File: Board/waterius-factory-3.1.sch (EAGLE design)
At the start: 23 parts, among them IC1 TINY85-20SU, U3 ESP01

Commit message: New attiny package
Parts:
- IC1: value TINY85-20SU -> ATTINY85-20SU; device atmel:TINY13-20SU -> attiny85:ATTINY85-20SU
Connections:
- net +3V: now also IC1P.VCC; no longer IC1.VCC
- net GND: now also IC1P.GND; no longer IC1.GND
- net IN1: now also IC1G$1.PB3(ADC3/!OC1B!/CLKI/XTAL1/PCINT3); no longer IC1.PB3/PCINT3/CLKI/ADC3
- net IN2: now also IC1G$1.PB4(ADC2/OC1B/CLKO/XTAL2/PCINT4); no longer IC1.PB4/PCINT4/ADC2
- net PRG_RST: now also IC1G$1.PB5(DW/ADC0/!RESET!/PCINT5); no longer IC1.PB5/PCINT5/!RESET!/ADC0/DW
- net SCK: now also IC1G$1.PB2(SCK/USCK/SCL/ADC1/T0/INT0/PCINT2); no longer IC1.PB2/PCINT2/SCK/ADC1/T0
- net SDA: now also IC1G$1.PB0(MOSI/DI/SDA/AIN0/OC0A/!OC1A!/AREF/PCINT0); no longer IC1.PB0/PCINT0/AIN0/OC0A/MOSI
- net WAKE_UP: now also IC1G$1.PB1(MISO/DO/AIN1/OC0B/OC1A/PCINT1); no longer IC1.PB1/PCINT1/AIN1/OC0B/INT0/MISO
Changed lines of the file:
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@@
 <part name="C4" library="rcl" deviceset="C-EU" device="C0805" value="1uF"/>
 <part name="C2" library="rcl" deviceset="C-EU" device="C0805" value="0.1uF"/>
-<part name="+3V" library="supply1" library_urn="urn:adsk.eagle:library:371" deviceset="VCC" device=""/>
+<part name="+3V" library="supply1" deviceset="VCC" device=""/>
 <part name="X1" library="con-wago255" deviceset="233-104" device=""/>
 <part name="R1" library="resistor" deviceset="R-EU_" device="R0805" value="3k3"/>
 <part name="GND1" library="supply1" deviceset="GND" device=""/>
 <part name="GND2" library="supply1" deviceset="GND" device=""/>
-<part name="+3V2" library="supply1" library_urn="urn:adsk.eagle:library:371" deviceset="VCC" device=""/>
+<part name="+3V2" library="supply1" deviceset="VCC" device=""/>
 <part name="LOG" library="pinhead" deviceset="PINHD-1X1" device=""/>
 <part name="R3" library="resistor" deviceset="R-EU_" device="R0805" value="300"/>
@@
 <part name="GND5" library="supply1" deviceset="GND" device=""/>
 <part name="RST" library="pinhead" deviceset="PINHD-1X1" device="" value="RST"/>
-<part name="IC1" library="atmel" deviceset="TINY13" device="SU" technology="-20" value="TINY85-20SU"/>
 <part name="R5" library="resistor" deviceset="R-EU_" device="R0805" value="3k3"/>
 <part name="C3" library="rcl" deviceset="C-EU" device="C0805" value="0.1uF"/>
@@
 <part name="U$1" library="MCP1700T-3002E_TT" deviceset="MCP1700T-3002E/TT" device=""/>
 <part name="S1" library="switch-omron" library_urn="urn:adsk.eagle:library:377" deviceset="31-XX" device="" package3d_urn="urn:adsk.eagle:package:27487/1"/>
+<part name="IC1" library="attiny85" deviceset="ATTINY*5" device="-20SU" technology="8"/>
 </parts>
 <sheets>
@@
 <attribute name="VALUE" x="64.77" y="25.4" size="1.778" layer="96" rot="R180"/>
 </instance>
-<instance part="IC1" gate="G$1" x="109.22" y="22.86" smashed="yes">
-<attribute name="NAME" x="91.44" y="39.37" size="1.778" layer="95"/>
-<attribute name="VALUE" x="91.44" y="12.7" size="1.778" layer="96"/>
-</instance>
 <instance part="R5" gate="G$1" x="76.2" y="45.72" smashed="yes" rot="R90">
 <attribute name="NAME" x="74.7014" y="41.91" size="1.778" layer="95" rot="R90"/>
@@
 <attribute name="NAME" x="36.83" y="27.305" size="1.778" layer="95" rot="MR270"/>
 <attribute name="VALUE" x="39.37" y="22.225" size="1.778" layer="96" rot="MR270"/>
+</instance>
+<instance part="IC1" gate="G$1" x="127" y="27.94" smashed="yes" rot="MR180">
+<attribute name="NAME" x="96.52" y="17.272" size="1.778" layer="95" ratio="10" rot="SMR180"/>
+<attribute name="VALUE" x="96.52" y="36.068" size="1.778" layer="96" ratio="10" rot="SMR180" align="top-left"/>
+</instance>
+<instance part="IC1" gate="P" x="162.56" y="27.94" smashed="yes">
+<attribute name="NAME" x="162.052" y="27.94" size="1.778" layer="95" rot="R90" align="bottom-center"/>
 </instance>
 </instances>
@@
 <wire x1="76.2" y1="53.34" x2="76.2" y2="50.8" width="0.1524" layer="91"/>
 <junction x="43.18" y="53.34"/>
-<pinref part="IC1" gate="G$1" pin="VCC"/>
-<wire x1="88.9" y1="35.56" x2="81.28" y2="35.56" width="0.1524" layer="91"/>
-<wire x1="81.28" y1="35.56" x2="81.28" y2="53.34" width="0.1524" layer="91"/>
-<wire x1="81.28" y1="53.34" x2="76.2" y2="53.34" width="0.1524" layer="91"/>
+<pinref part="IC1" gate="P" pin="VCC"/>
+<wire x1="76.2" y1="53.34" x2="162.56" y2="53.34" width="0.1524" layer="91"/>
+<wire x1="162.56" y1="53.34" x2="162.56" y2="35.56" width="0.1524" layer="91"/>
 <junction x="76.2" y="53.34"/>
 </segment>
@@
 </segment>
 <segment>
-<pinref part="IC1" gate="G$1" pin="PB3/PCINT3/CLKI/ADC3"/>
-<wire x1="88.9" y1="25.4" x2="68.58" y2="25.4" width="0.1524" layer="91"/>
+<wire x1="91.44" y1="25.4" x2="68.58" y2="25.4" width="0.1524" layer="91"/>
 <label x="68.58" y="25.4" size="1.778" layer="95"/>
+<pinref part="IC1" gate="G$1" pin="PB3(ADC3/!OC1B!/CLKI/XTAL1/PCINT3)"/>
 </segment>
 </net>
@@
 </segment>
 <segment>
-<pinref part="IC1" gate="G$1" pin="PB4/PCINT4/ADC2"/>
-<wire x1="88.9" y1="22.86" x2="68.58" y2="22.86" width="0.1524" layer="91"/>
+<wire x1="91.44" y1="22.86" x2="68.58" y2="22.86" width="0.1524" layer="91"/>
 <label x="68.58" y="22.86" size="1.778" layer="95"/>
+<pinref part="IC1" gate="G$1" pin="PB4(ADC2/OC1B/CLKO/XTAL2/PCINT4)"/>
 </segment>
 </net>
@@
 </segment>
 <segment>
-<pinref part="IC1" gate="G$1" pin="GND"/>
-<wire x1="88.9" y1="17.78" x2="86.36" y2="17.78" width="0.1524" layer="91"/>
-<wire x1="86.36" y1="17.78" x2="86.36" y2="7.62" width="0.1524" layer="91"/>
-<wire x1="86.36" y1="7.62" x2="76.2" y2="7.62" width="0.1524" layer="91"/>
 <pinref part="C3" gate="G$1" pin="2"/>
-<wire x1="76.2" y1="7.62" x2="76.2" y2="10.16" width="0.1524" layer="91"/>
 <pinref part="GND7" gate="1" pin="GND"/>
 <wire x1="76.2" y1="5.08" x2="76.2" y2="7.62" width="0.1524" layer="91"/>
+<wire x1="76.2" y1="7.62" x2="76.2" y2="10.16" width="0.1524" layer="91"/>
+<wire x1="76.2" y1="7.62" x2="162.56" y2="7.62" width="0.1524" layer="91"/>
+<wire x1="162.56" y1="7.62" x2="162.56" y2="20.32" width="0.1524" layer="91"/>
 <junction x="76.2" y="7.62"/>
+<pinref part="IC1" gate="P" pin="GND"/>
 </segment>
 </net>
@@
 </segment>
 <segment>
-<pinref part="IC1" gate="G$1" pin="PB0/PCINT0/AIN0/OC0A/MOSI"/>
-<wire x1="88.9" y1="33.02" x2="68.58" y2="33.02" width="0.1524" layer="91"/>
+<wire x1="91.44" y1="33.02" x2="68.58" y2="33.02" width="0.1524" layer="91"/>
 <label x="68.58" y="33.02" size="1.778" layer="95"/>
+<pinref part="IC1" gate="G$1" pin="PB0(MOSI/DI/SDA/AIN0/OC0A/!OC1A!/AREF/PCINT0)"/>
 </segment>
 </net>
@@
 </segment>
 <segment>
-<pinref part="IC1" gate="G$1" pin="PB2/PCINT2/SCK/ADC1/T0"/>
-<wire x1="88.9" y1="27.94" x2="68.58" y2="27.94" width="0.1524" layer="91"/>
+<wire x1="91.44" y1="27.94" x2="68.58" y2="27.94" width="0.1524" layer="91"/>
 <label x="68.58" y="27.94" size="1.778" layer="95"/>
+<pinref part="IC1" gate="G$1" pin="PB2(SCK/USCK/SCL/ADC1/T0/INT0/PCINT2)"/>
 </segment>
 </net>
@@
 </segment>
 <segment>
-<pinref part="IC1" gate="G$1" pin="PB1/PCINT1/AIN1/OC0B/INT0/MISO"/>
-<wire x1="88.9" y1="30.48" x2="68.58" y2="30.48" width="0.1524" layer="91"/>
+<wire x1="91.44" y1="30.48" x2="68.58" y2="30.48" width="0.1524" layer="91"/>
 <label x="68.58" y="30.48" size="1.778" layer="95"/>
+<pinref part="IC1" gate="G$1" pin="PB1(MISO/DO/AIN1/OC0B/OC1A/PCINT1)"/>
 </segment>
 </net>
@@
 <pinref part="C3" gate="G$1" pin="1"/>
 <wire x1="76.2" y1="40.64" x2="76.2" y2="20.32" width="0.1524" layer="91"/>
-<pinref part="IC1" gate="G$1" pin="PB5/PCINT5/!RESET!/ADC0/DW"/>
 <wire x1="76.2" y1="20.32" x2="76.2" y2="17.78" width="0.1524" layer="91"/>
-<wire x1="88.9" y1="20.32" x2="76.2" y2="20.32" width="0.1524" layer="91"/>
+<wire x1="91.44" y1="20.32" x2="76.2" y2="20.32" width="0.1524" layer="91"/>
 <junction x="76.2" y="20.32"/>
 <pinref part="RST" gate="G$1" pin="1"/>
 <wire x1="60.96" y1="20.32" x2="76.2" y2="20.32" width="0.1524" layer="91"/>
-</segment>
-</net>
+<pinref part="IC1" gate="G$1" pin="PB5(DW/ADC0/!RESET!/PCINT5)"/>
+</segment>
+</net>

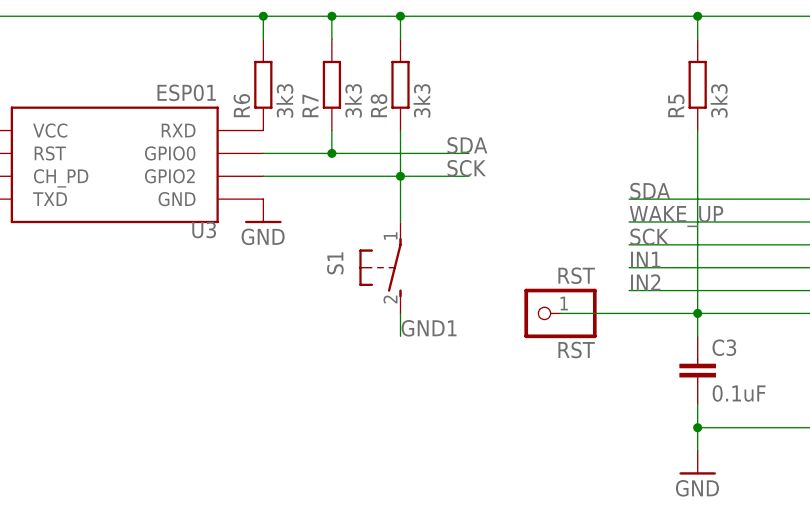
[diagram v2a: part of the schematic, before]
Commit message: Connected the button housing to GND
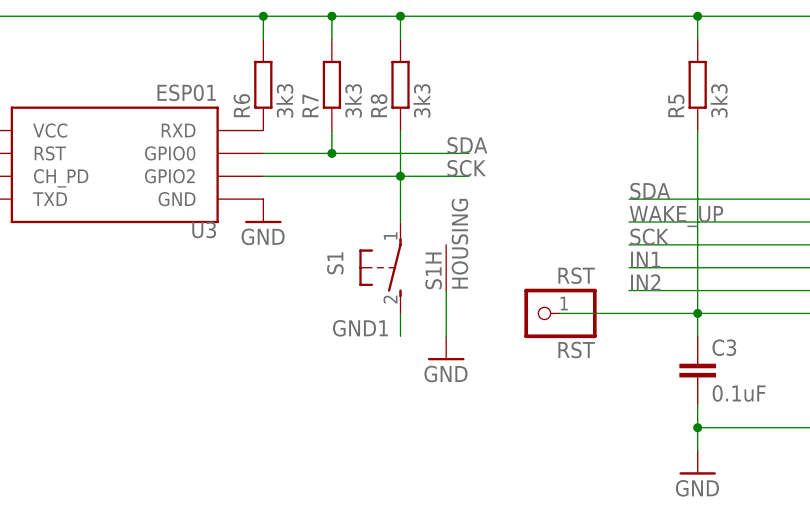
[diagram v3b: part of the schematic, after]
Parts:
- S1: device switch-omron:31-XX -> switch-31-XX:31-XX
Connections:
- net GND: now also S1H.HOUSING
- net GND1: now also S11.S; no longer S1.S
- net SCK: now also S11.P; no longer S1.P
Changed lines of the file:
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@@
 <?xml version="1.0" encoding="utf-8"?>
 <!DOCTYPE eagle SYSTEM "eagle.dtd">
-<eagle version="9.0.1">
+<eagle version="9.6.2">
 <drawing>
 <settings>
@@
 <part name="GND7" library="supply1" deviceset="GND" device=""/>
 <part name="U$1" library="MCP1700T-3002E_TT" deviceset="MCP1700T-3002E/TT" device=""/>
-<part name="S1" library="switch-omron" library_urn="urn:adsk.eagle:library:377" deviceset="31-XX" device="" package3d_urn="urn:adsk.eagle:package:27487/1"/>
+<part name="S1" library="switch-31-XX" deviceset="31-XX" device="" package3d_urn="urn:adsk.eagle:package:27487/1"/>
 <part name="IC1" library="attiny85" deviceset="ATTINY*5" device="-20SU" technology="8"/>
+<part name="GND6" library="supply1" deviceset="GND" device=""/>
 </parts>
 <sheets>
@@
 <instance part="IC1" gate="P" x="162.56" y="27.94" smashed="yes">
 <attribute name="NAME" x="162.052" y="27.94" size="1.778" layer="95" rot="R90" align="bottom-center"/>
+</instance>
+<instance part="S1" gate="H" x="48.26" y="22.86" smashed="yes">
+<attribute name="NAME" x="47.752" y="22.86" size="1.778" layer="95" rot="R90"/>
+</instance>
+<instance part="GND6" gate="1" x="48.26" y="15.24" smashed="yes">
+<attribute name="VALUE" x="45.72" y="12.7" size="1.778" layer="96"/>
 </instance>
 </instances>
@@
 </segment>
 <segment>
-<label x="43.18" y="17.78" size="1.778" layer="95"/>
+<label x="35.56" y="17.78" size="1.778" layer="95"/>
 <wire x1="43.18" y1="17.78" x2="43.18" y2="20.32" width="0.1524" layer="91"/>
 <pinref part="S1" gate="1" pin="S"/>
@@
 <pinref part="IC1" gate="P" pin="GND"/>
 </segment>
+<segment>
+<pinref part="GND6" gate="1" pin="GND"/>
+<pinref part="S1" gate="H" pin="HOUSING"/>
+<wire x1="48.26" y1="17.78" x2="48.26" y2="22.86" width="0.1524" layer="91"/>
+</segment>
 </net>
 <net name="N$3" class="0">
@@
 </drawing>
 <compatibility>
-<note version="8.2" severity="warning">
-Since Version 8.2, EAGLE supports online libraries. The ids
-of those online libraries will not be understood (or retained)
-with this version.
-</note>
 <note version="8.3" severity="warning">
 Since Version 8.3, EAGLE supports URNs for individual library
